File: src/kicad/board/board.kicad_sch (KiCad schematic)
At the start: 19 parts, among them U1 Pico

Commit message: update pcb
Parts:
- removed J?: Micro_SD_Card, symbol Connector:Micro_SD_Card
- added J2: Micro_SD_Card_Det, Connector_Card:microSD_HC_Molex_104031-0811, symbol Connector:Micro_SD_Card_Det
- C1, C2, C3, C4, C5, C6: renamed from C?; footprint (none) -> Capacitor_SMD:C_0805_2012Metric
- R1, R2, R3, R4, R5, R6, R7: renamed from R?; footprint (none) -> Resistor_SMD:R_0805_2012Metric
- U2: renamed from U?; footprint (none) -> Library:MAX98357
- gave numbers to parts that had none: 3
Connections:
- net +3.3V: now also J2.4 (VDD)
- net GND: now also J2.11 (SHIELD), J2.6 (VSS)
- net SD_CLK: now also J2.5 (CLK)
- net SD_CS: now also J2.2 (DAT3/CD)
- net SD_MISO: now also J2.7 (DAT0)
- net SD_MOSI: now also J2.3 (CMD)
- net VDD: now also U1.39 (VSYS), U2.2 (GAIN)
- net at R7.2: now also J2.1 (DAT2)
- net Power2/USB_VBUS: now reaches U1.40 (VBUS)
- net at R2.2: now also J2.8 (DAT1)
- net GP10: no longer names the net of U1.14 (GPIO10)
- net GP11: no longer names the net of U1.15 (GPIO11)
- no-connect marks 1 -> 31
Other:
- removed sheet Power
- added sheet Power2 (power2.kicad_sch)
- note added: "VDD=6DB"
- note removed: "5V and 1M resistor -> left/2 + right/2"
- note removed: "5v?"
- note removed: "Default=9DB"
- moved on the sheet: C1, C2, C3, C4, C5, C6, FB1, FB2, J1, R1, R2, R3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

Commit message: update wip
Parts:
- FB1, FB2: footprint (none) -> Library:Ferrite-0805
- J1: footprint (none) -> TerminalBlock:TerminalBlock_bornier-2_P5.08mm
- U1: footprint RPi_Pico:RPi_Pico_SMD_TH -> Library:RPI_PICO_smd
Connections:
- net GND: now also U2.17 (THERMAL); no longer U2.THERMAL (GND)

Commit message: update
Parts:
- removed R1: 1M, Resistor_SMD:R_0805_2012Metric, symbol Device:R
- added J3: Conn_01x06, Connector_PinHeader_2.54mm:PinHeader_1x06_P2.54mm_Vertical, symbol Connector_Generic:Conn_01x06
- C1, C5: Vendor (none) -> C15850
- C2, C6: Vendor (none) -> C28233
- C3, C4: Vendor (none) -> C107145
- FB1, FB2: Vendor (none) -> C1015
- J2: Vendor (none) -> C585350
- R2, R3, R4, R5, R6, R7: Vendor (none) -> C17673
- U2: footprint Library:MAX98357 -> Package_DFN_QFN:TQFN-16-1EP_3x3mm_P0.5mm_EP1.6x1.6mm; Vendor (none) -> C910544
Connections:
- net GND: now also U1.13 (GND), U1.18 (GND), U1.23 (GND), U1.28 (GND), U1.3 (GND), U1.33 (AGND), U1.38 (GND), U1.8 (GND), J3.1 (Pin_1)
- net VDD: now also U2.4 (~{SD_MODE})
- net at U1.21 (GPIO16): now also J3.6 (Pin_6)
- net at U1.22 (GPIO17): now also J3.5 (Pin_5)
- net at U1.24 (GPIO18): now also J3.4 (Pin_4)
- net at U1.25 (GPIO19): now also J3.3 (Pin_3)
- net at U1.26 (GPIO20): now also J3.2 (Pin_2)
- no-connect marks 31 -> 18
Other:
- note added: "Left channel only"

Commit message: update
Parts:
- removed C1: 10uF, Capacitor_SMD:C_0805_2012Metric, symbol Device:C
- removed C2: 0.1uF, Capacitor_SMD:C_0805_2012Metric, symbol Device:C
- removed C3, C4: 220pF, Capacitor_SMD:C_0805_2012Metric, symbol Device:C
- removed FB1, FB2: Ferrite, Library:Ferrite-0805, symbol Device:FerriteBead_Small
- removed J1: Screw_Terminal_Speaker, TerminalBlock:TerminalBlock_bornier-2_P5.08mm, symbol Connector:Screw_Terminal_01x02
- removed U2: MAX98357, Package_DFN_QFN:TQFN-16-1EP_3x3mm_P0.5mm_EP1.6x1.6mm, symbol project_library:MAX98357
- added J3, J4: Conn_01x06_Male, Connector_JST:JST_PH_B6B-PH-SM4-TB_1x06-1MP_P2.00mm_Vertical, symbol Connector:Conn_01x06_Male
- renumbered C5 to C1, C6 to C2, J2 to J1, J3 to J2, R2 to R1, R3 to R2, R4 to R3, R5 to R4, R6 to R5, R7 to R6
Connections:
- net +3.3V: now also J3.2 (Pin_2)
- net GND: now also J2.2 (Pin_2), J3.1 (Pin_1)
- net GP12: now also J3.5 (Pin_5)
- net GP13: now also J3.4 (Pin_4)
- net GP14: now also J3.3 (Pin_3)
- net GP15: now also J3.6 (Pin_6)
- net at U1.26 (GPIO20): no longer J2.2 (Pin_2)
- net at J2.3 (Pin_3): now also U1.5 (GPIO3); no longer U1.25 (GPIO19)
- net at J2.4 (Pin_4): now also U1.4 (GPIO2); no longer U1.24 (GPIO18)
- net at J2.5 (Pin_5): now also U1.2 (GPIO1); no longer U1.22 (GPIO17)
- net at J2.6 (Pin_6): now also U1.1 (GPIO0); no longer U1.21 (GPIO16)
- net Sound/SPEAKER_EN: now reaches U1.29 (GPIO22)
- net VDD renamed Power/OUT
- new net Input/3.3V_LOCAL: J4.2 (Pin_2)
- new net Input/A: J4.6 (Pin_6)
- new net Input/GND_LOCAL: J4.1 (Pin_1)
- new net Input/S0: J4.5 (Pin_5)
- new net Input/S1: J4.4 (Pin_4)
- new net Input/S2: J4.3 (Pin_3)
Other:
- sheet Power2 renamed Power
- added sheet Sound (sound.kicad_sch)
- sheet Input ports: added 3.3V_LOCAL, GND_LOCAL; removed none
- note added: "TODO: optimize pin config"
- note removed: "Left channel only"
- note removed: "TODO: make sure this pin config is nice"
- note removed: "VDD=6DB"
- note removed: "https://cdn-learn.adafruit.com/downloads/pdf/adafruit-max98357-i2s-class-d-mono-amp.pdf"
- note removed: "https://datasheets.raspberrypi.com/pico/pico-datasheet.pdf#powerchain-section"
- moved on the sheet: J2, U1

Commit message: update
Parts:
- J3, J4: Vendor (none) -> C265088
- R1, R2, R3, R4, R5, R6: Vendor C17673 -> C17713
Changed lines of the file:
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@@
       (effects (font (size 1.27 1.27)) hide)
     )
-    (property "Vendor" "C17673" (id 4) (at 74.93 139.7 0)
+    (property "Vendor" "C17713" (id 4) (at 74.93 139.7 0)
       (effects (font (size 1.27 1.27)) hide)
     )
@@
       (effects (font (size 1.27 1.27)) hide)
     )
-    (property "Vendor" "C17673" (id 4) (at 82.55 139.7 0)
+    (property "Vendor" "C17713" (id 4) (at 82.55 139.7 0)
       (effects (font (size 1.27 1.27)) hide)
     )
@@
       (effects (font (size 1.27 1.27)) hide)
     )
-    (property "Vendor" "C17673" (id 4) (at 72.39 139.7 0)
+    (property "Vendor" "C17713" (id 4) (at 72.39 139.7 0)
       (effects (font (size 1.27 1.27)) hide)
     )
@@
       (effects (font (size 1.27 1.27)) hide)
     )
-    (property "Vendor" "C17673" (id 4) (at 69.85 139.7 0)
+    (property "Vendor" "C17713" (id 4) (at 69.85 139.7 0)
       (effects (font (size 1.27 1.27)) hide)
     )
@@
       (effects (font (size 1.27 1.27)) hide)
     )
+    (property "Vendor" "C265088" (id 4) (at 200.66 99.06 0)
+      (effects (font (size 1.27 1.27)) hide)
+    )
     (pin "1")
     (pin "2")
@@
       (effects (font (size 1.27 1.27)) hide)
     )
-    (property "Vendor" "C17673" (id 4) (at 77.47 139.7 0)
+    (property "Vendor" "C17713" (id 4) (at 77.47 139.7 0)
       (effects (font (size 1.27 1.27)) hide)
     )
@@
     )
     (property "Datasheet" "~" (id 3) (at 213.36 96.52 0)
+      (effects (font (size 1.27 1.27)) hide)
+    )
+    (property "Vendor" "C265088" (id 4) (at 213.36 96.52 0)
       (effects (font (size 1.27 1.27)) hide)
     )
@@
       (effects (font (size 1.27 1.27)) hide)
     )
-    (property "Vendor" "C17673" (id 4) (at 80.01 139.7 0)
+    (property "Vendor" "C17713" (id 4) (at 80.01 139.7 0)
       (effects (font (size 1.27 1.27)) hide)
     )
@@
       (reference "J7") (unit 1) (value "Screw_Terminal_Speaker") (footprint "TerminalBlock:TerminalBlock_bornier-2_P5.08mm")
     )
+    (path "/d540bb9b-d45f-4ddd-b651-2c00d8abffca/6e5ac643-a1f5-4f29-845b-2b375098768f"
+      (reference "J8") (unit 1) (value "Conn_01x02_Male") (footprint "Connector_PinHeader_2.54mm:PinHeader_1x02_P2.54mm_Vertical")
+    )
     (path "/d540bb9b-d45f-4ddd-b651-2c00d8abffca/747c2690-a6dd-4c28-be61-b1de1b1c2844"

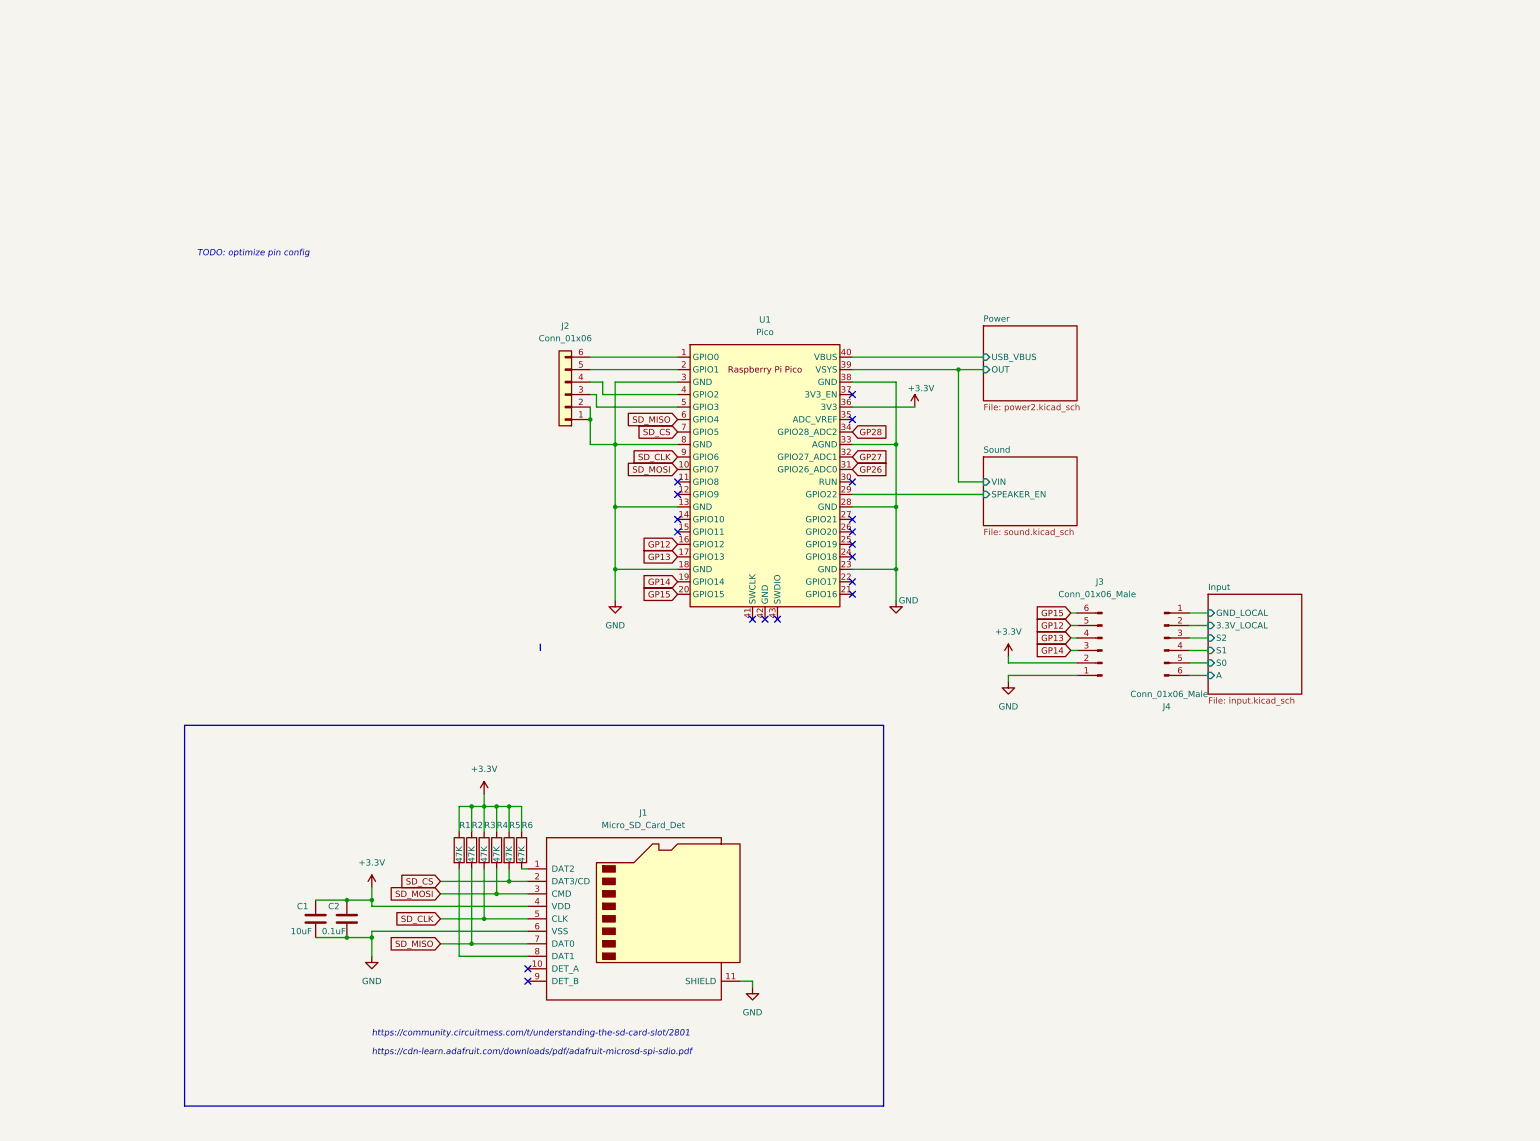
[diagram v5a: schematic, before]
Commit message: update with rp2040, instead of rpi pico. wip
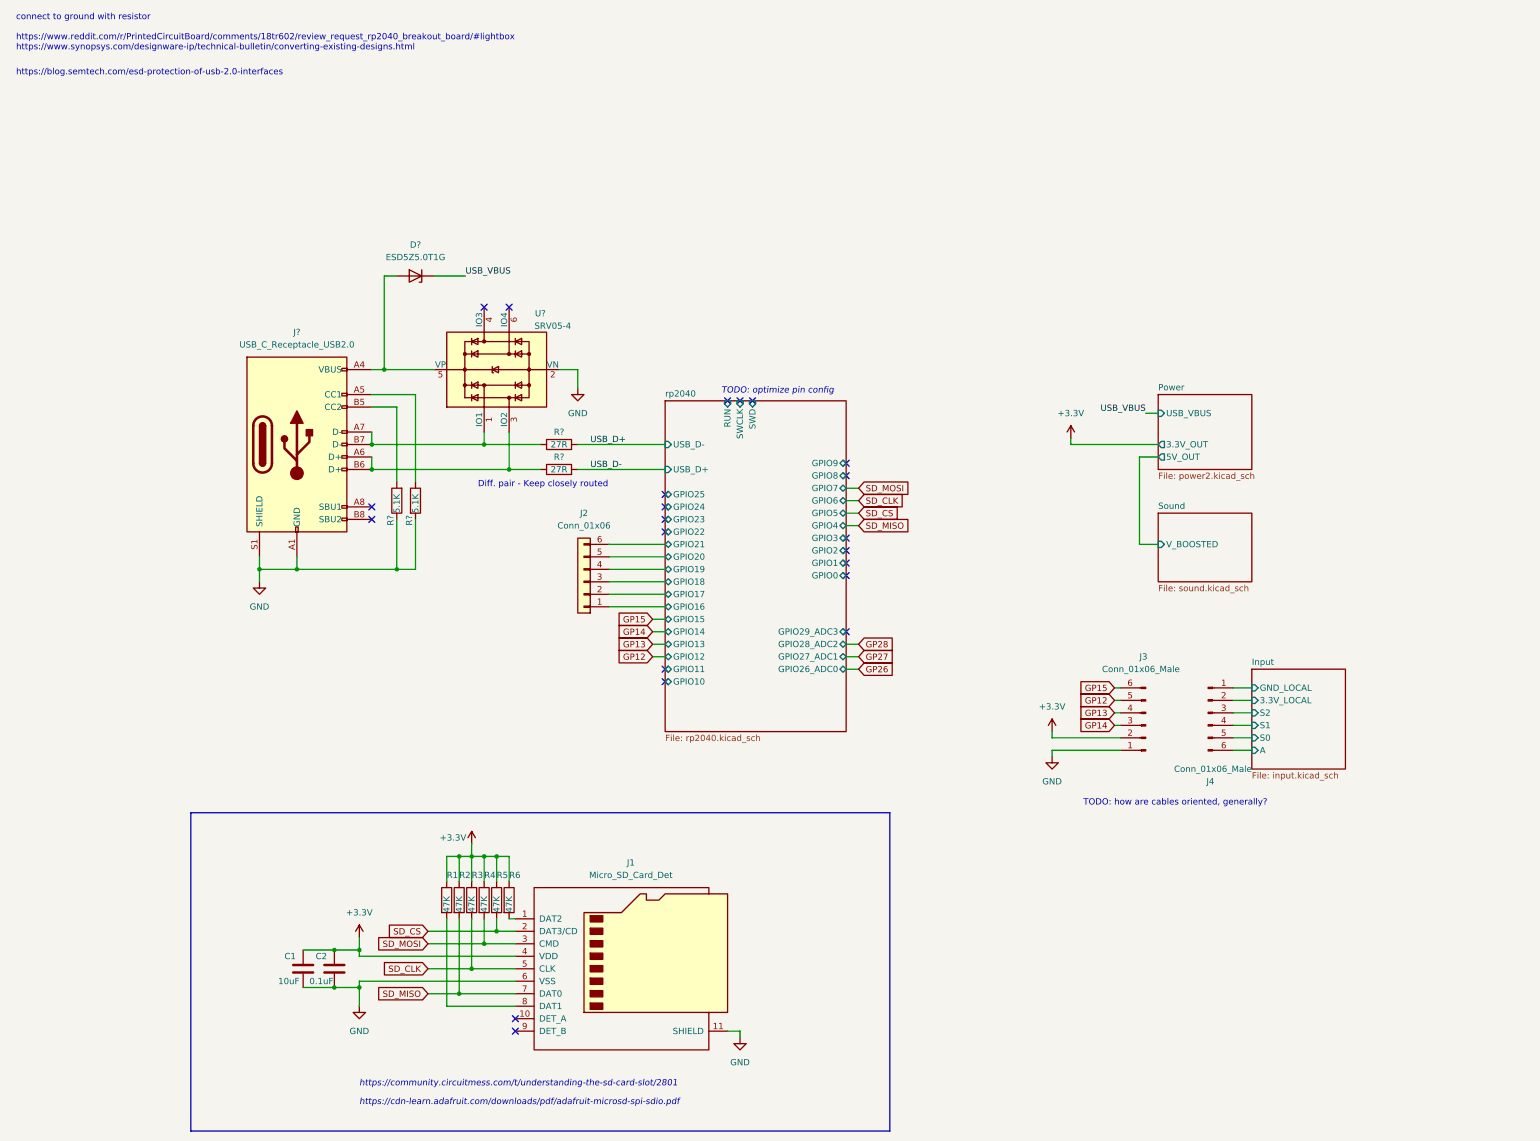
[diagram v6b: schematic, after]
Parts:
- removed U1: Pico, Library:RPI_PICO_smd, symbol MCU_RaspberryPi_and_Boards:Pico
- added D?: ESD5Z5.0T1G, Diode_SMD:D_SOD-523, symbol Diode:ESD5Zxx
- added J?: USB_C_Receptacle_USB2.0, symbol Connector:USB_C_Receptacle_USB2.0
- added R? (x2): 27R, symbol Device:R
- added R? (x2): 5.1K, symbol Device:R
- added U?: SRV05-4, Package_TO_SOT_SMD:SOT-23-6, symbol Power_Protection:SRV05-4
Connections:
- net GND: now also J?.A1 (GND), J?.A12 (GND), J?.B1 (GND), J?.B12 (GND), J?.S1 (SHIELD), R?.1, R?.2, U?.2 (VN); no longer J2.1 (Pin_1), J2.2 (Pin_2)
- net rp2040/GPIO18: now reaches J2.3 (Pin_3)
- net rp2040/GPIO19: now reaches J2.4 (Pin_4)
- net rp2040/GPIO20: now reaches J2.5 (Pin_5)
- net rp2040/GPIO21: now reaches J2.6 (Pin_6)
- new net: J?.A6 (D+), J?.B6 (D+), R?.1, U?.3 (IO2)
- new net: J?.A7 (D-), J?.B7 (D-), R?.1, U?.1 (IO1)
- new net: D?.2 (A), J?.A4 (VBUS), J?.A9 (VBUS), J?.B4 (VBUS), J?.B9 (VBUS), U?.5 (VP)
- new net: J?.B5 (CC2), R?.2
- new net: J?.A5 (CC1), R?.1
- new net USB_D+: R?.2
- new net USB_D-: R?.2
- new net USB_VBUS: D?.1 (K)
- new net rp2040/GPIO16: J2.1 (Pin_1)
- new net rp2040/GPIO17: J2.2 (Pin_2)
- no-connect marks 18 -> 22
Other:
- added sheet rp2040 (rp2040.kicad_sch)
- sheet Power ports: added 3.3V_OUT, 5V_OUT; removed OUT
- sheet Sound ports: added V_BOOSTED; removed SPEAKER_EN, VIN
- note added: "Diff. pair - Keep closely routed"
- note added: "TODO: how are cables oriented, generally?"
- note added: "connect to ground with resistor https://www.reddit.com/r/PrintedCircuitBoard/comments/18tr602/review_request_rp2040_breakout_board/#lightbox https://www.synopsys.com/designware-ip/technical-bulletin/converting-existing-designs.html"
- note added: "https://blog.semtech.com/esd-protection-of-usb-2.0-interfaces"
- moved on the sheet: C1, C2, J1, J2, J3, J4, R1, R2, R3, R4, R5, R6

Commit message: update
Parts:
- D1: renamed from D?; Vendor (none) -> C5199848
- J1: renamed from J?; footprint (none) -> Connector_USB:USB_C_Receptacle_G-Switch_GT-USB-7010ASV; Vendor (none) -> C2988369
- R1, R2: renamed from R?; footprint (none) -> Resistor_SMD:R_0805_2012Metric; Vendor (none) -> C27834
- R10, R9: renamed from R?; footprint (none) -> Resistor_SMD:R_0805_2012Metric; Vendor (none) -> C17594
- gave numbers to parts that had none: 1
- renumbered J1 to J3, J3 to J4, J4 to J5, R1 to R3, R2 to R4, R3 to R5, R4 to R6, R5 to R7, R6 to R8
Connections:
- net Input/A: no longer names the net of J5.6 (Pin_6)
- net Input/S0 renamed Input/SCK
- net Input/S1 renamed Input/SDA
- net Input/S2 renamed Input/INT
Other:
- sheet Input ports: added INT, SCK, SDA; removed A, S0, S1, S2
- note added: "https://blog.semtech.com/esd-protection-of-usb-2.0-interfaces https://files.seeedstudio.com/wiki/XIAO-RP2040/res/Seeed-Studio-XIAO-RP2040-v1.3.pdf"
- note removed: "https://blog.semtech.com/esd-protection-of-usb-2.0-interfaces"

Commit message: update
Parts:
- removed D1: ESD5Z5.0T1G, Diode_SMD:D_SOD-523, symbol Diode:ESD5Zxx
- removed J4, J5: Conn_01x06_Male, Connector_JST:JST_PH_B6B-PH-SM4-TB_1x06-1MP_P2.00mm_Vertical, symbol Connector:Conn_01x06_Male
- removed U1: SRV05-4, Package_TO_SOT_SMD:SOT-23-6, symbol Power_Protection:SRV05-4
- added D? (x3): DF2S6.8FS, Diode_SMD:D_SOD-923, symbol Device:D_Schottky
- added J? (x2): Conn_01x05_Male, Connector_JST:JST_PH_B5B-PH-SM4-TB_1x05-1MP_P2.00mm_Vertical, symbol Connector:Conn_01x05_Male
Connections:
- net +3.3V: now also J?.2 (Pin_2)
- net GND: now also D?.2 (A), D?.2 (A), D?.2 (A), J?.1 (Pin_1)
- net Input/3.3V_LOCAL: now also J?.2 (Pin_2)
- net Input/GND_LOCAL: now also J?.1 (Pin_1)
- net Input/INT: now also J?.3 (Pin_3)
- net Input/SCK: now also J?.5 (Pin_5)
- net Input/SDA: now also J?.4 (Pin_4)
- net USB_VBUS: now also J1.A4 (VBUS), J1.A9 (VBUS), J1.B4 (VBUS), J1.B9 (VBUS), D?.1 (K)
- net at J1.A6 (D+), J1.B6 (D+), R10.1: now also D?.1 (K)
- net at J1.A7 (D-), J1.B7 (D-), R9.1: now also D?.1 (K)
- new net INT: J?.3 (Pin_3)
- new net RP2040_SCL: J?.5 (Pin_5)
- new net RP2040_SDA: J?.4 (Pin_4)
- no-connect marks 22 -> 16
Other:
- sheet rp2040 ports: added none; removed RUN
- moved on the sheet: J2
